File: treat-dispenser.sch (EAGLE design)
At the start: 39 parts, among them U1 MCP73831, U2 TPS61032, U3 ATMEGA32U4, Y1 16MHz

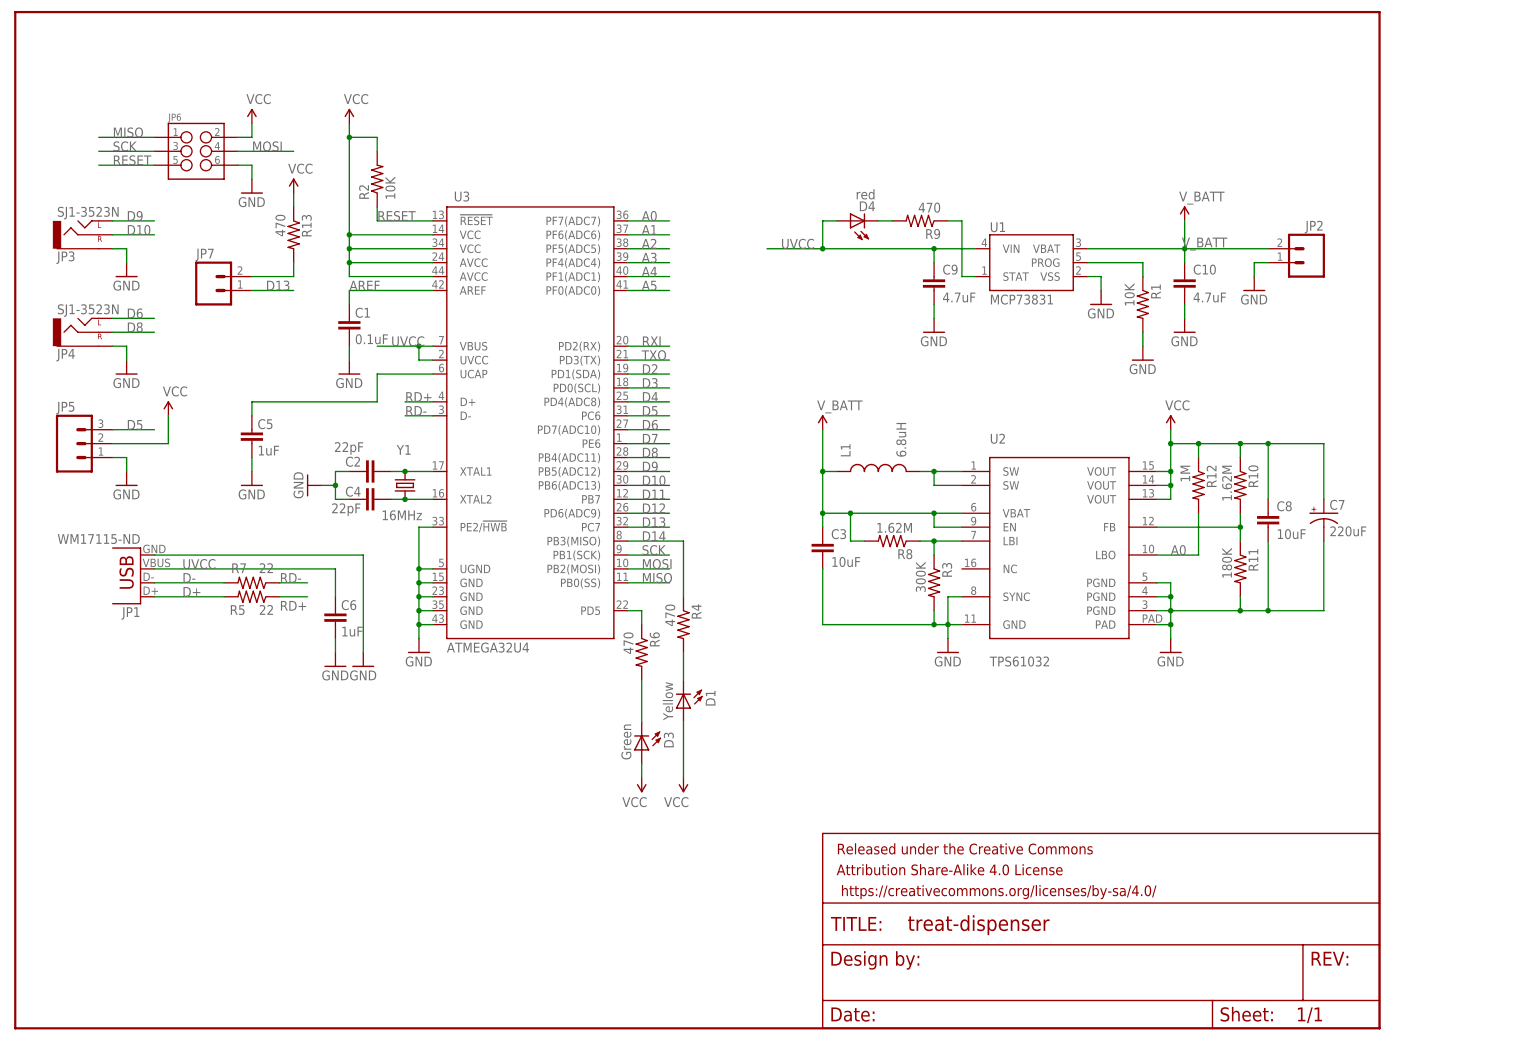
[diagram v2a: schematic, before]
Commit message: added optional sensor, cleaned up for mfg
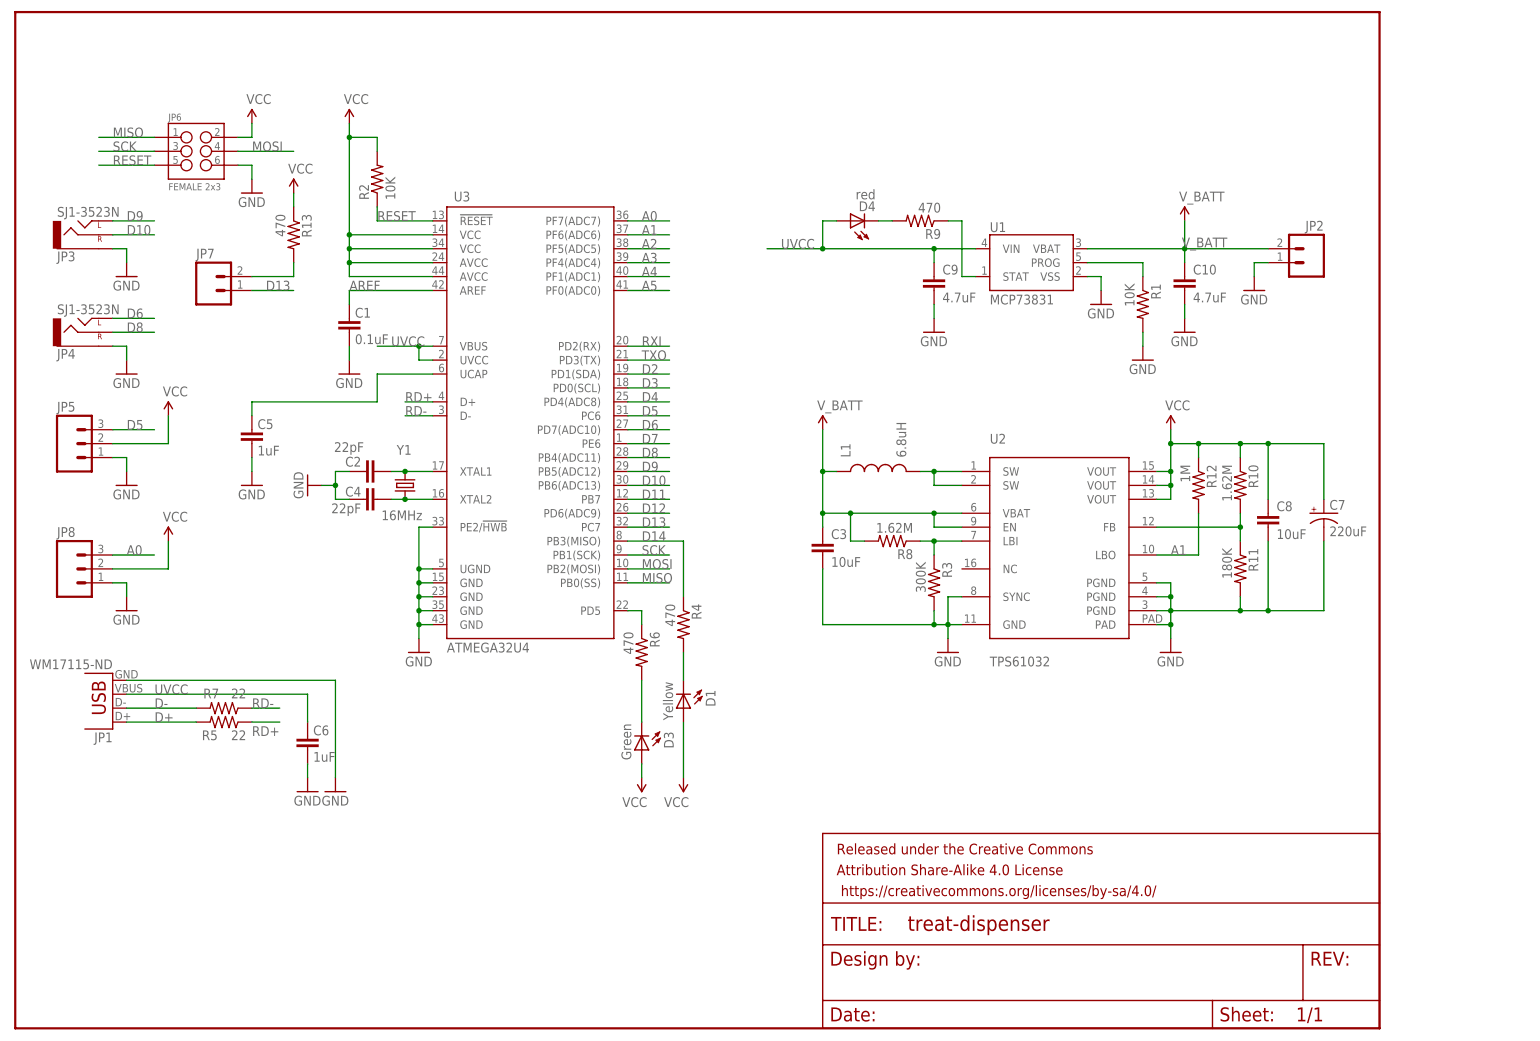
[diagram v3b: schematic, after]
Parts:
- added JP8: (no value), SparkFun-Connectors:M03PTH
- JP6: value (none) -> FEMALE 2x3; device SparkFun-Connectors:M03X2POGO_PINS -> SparkFun-Connectors:M03X2FEMALE
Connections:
- net A0: now also JP8.3; no longer R12.2, U2.LBO
- net A1: now also R12.2, U2.LBO
- net GND: now also JP8.1
- net VCC: now also JP8.2
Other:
- moved on the sheet: C6, JP1, R5, R7
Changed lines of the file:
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@@
 <part name="GND12" library="supply1" deviceset="GND" device=""/>
 <part name="R12" library="SparkFun" deviceset="RESISTOR" device="0603-RES" value="1M"/>
-<part name="JP6" library="SparkFun-Connectors" deviceset="M03X2" device="POGO_PINS"/>
 <part name="GND13" library="supply1" deviceset="GND" device=""/>
 <part name="C7" library="SparkFun-Capacitors" deviceset="CAP_POL" device="PTH1" value="220uF"/>
@@
 <part name="R13" library="SparkFun" deviceset="RESISTOR" device="0603-RES" value="470"/>
 <part name="SUPPLY7" library="SparkFun-Aesthetics" deviceset="VCC" device=""/>
+<part name="JP6" library="SparkFun-Connectors" deviceset="M03X2" device="FEMALE" value="FEMALE 2x3"/>
+<part name="JP8" library="SparkFun-Connectors" deviceset="M03" device="PTH"/>
+<part name="GND15" library="supply1" deviceset="GND" device=""/>
+<part name="SUPPLY8" library="SparkFun-Aesthetics" deviceset="VCC" device=""/>
 </parts>
 <sheets>
@@
 </instance>
 <instance part="GND6" gate="1" x="43.18" y="99.06"/>
-<instance part="C6" gate="G$1" x="58.42" y="76.2" smashed="yes" rot="R180">
-<attribute name="NAME" x="59.436" y="76.327" size="1.778" layer="95"/>
-<attribute name="VALUE" x="59.436" y="71.501" size="1.778" layer="96"/>
-</instance>
-<instance part="GND9" gate="1" x="58.42" y="66.04"/>
+<instance part="C6" gate="G$1" x="53.34" y="53.34" smashed="yes" rot="R180">
+<attribute name="NAME" x="54.356" y="53.467" size="1.778" layer="95"/>
+<attribute name="VALUE" x="54.356" y="48.641" size="1.778" layer="96"/>
+</instance>
+<instance part="GND9" gate="1" x="53.34" y="43.18"/>
 <instance part="R4" gate="G$1" x="121.92" y="73.66" rot="R270"/>
 <instance part="D1" gate="G$1" x="121.92" y="58.42" smashed="yes" rot="R180">
@@
 <attribute name="VALUE" x="118.237" y="63.246" size="1.778" layer="96" rot="R270"/>
 </instance>
-<instance part="R5" gate="G$1" x="43.18" y="78.74" smashed="yes" rot="R180">
-<attribute name="NAME" x="39.116" y="75.438" size="1.778" layer="95"/>
-<attribute name="VALUE" x="44.45" y="75.438" size="1.778" layer="96"/>
-</instance>
-<instance part="R7" gate="G$1" x="43.18" y="81.28" smashed="yes" rot="R180">
-<attribute name="NAME" x="39.37" y="83.058" size="1.778" layer="95"/>
-<attribute name="VALUE" x="44.45" y="83.058" size="1.778" layer="96"/>
-</instance>
-<instance part="GND3" gate="1" x="63.5" y="66.04"/>
+<instance part="R5" gate="G$1" x="38.1" y="55.88" smashed="yes" rot="R180">
+<attribute name="NAME" x="34.036" y="52.578" size="1.778" layer="95"/>
+<attribute name="VALUE" x="39.37" y="52.578" size="1.778" layer="96"/>
+</instance>
+<instance part="R7" gate="G$1" x="38.1" y="58.42" smashed="yes" rot="R180">
+<attribute name="NAME" x="34.29" y="60.198" size="1.778" layer="95"/>
+<attribute name="VALUE" x="39.37" y="60.198" size="1.778" layer="96"/>
+</instance>
+<instance part="GND3" gate="1" x="58.42" y="43.18"/>
 <instance part="P+1" gate="1" x="114.3" y="45.72" rot="R180"/>
 <instance part="P+2" gate="1" x="121.92" y="45.72" rot="R180"/>
-<instance part="JP1" gate="G$1" x="22.86" y="86.36" rot="R180"/>
+<instance part="JP1" gate="G$1" x="17.78" y="63.5" rot="R180"/>
 <instance part="C9" gate="G$1" x="167.64" y="134.62"/>
 <instance part="C10" gate="G$1" x="213.36" y="134.62"/>
@@
 <instance part="GND12" gate="1" x="20.32" y="137.16"/>
 <instance part="R12" gate="G$1" x="215.9" y="99.06" rot="R270"/>
-<instance part="JP6" gate="G$1" x="33.02" y="160.02"/>
 <instance part="GND13" gate="1" x="43.18" y="152.4"/>
 <instance part="C7" gate="G$1" x="238.76" y="93.98"/>
@@
 <instance part="R13" gate="G$1" x="50.8" y="144.78" rot="R270"/>
 <instance part="SUPPLY7" gate="G$1" x="50.8" y="152.4"/>
+<instance part="JP6" gate="G$1" x="33.02" y="160.02"/>
+<instance part="JP8" gate="G$1" x="10.16" y="83.82"/>
+<instance part="GND15" gate="1" x="20.32" y="76.2"/>
+<instance part="SUPPLY8" gate="G$1" x="27.94" y="88.9"/>
 </instances>
 <busses>
@@
 </segment>
 <segment>
-<wire x1="58.42" y1="71.12" x2="58.42" y2="68.58" width="0.1524" layer="91"/>
+<wire x1="53.34" y1="48.26" x2="53.34" y2="45.72" width="0.1524" layer="91"/>
 <pinref part="C6" gate="G$1" pin="1"/>
 <pinref part="GND9" gate="1" pin="GND"/>
 </segment>
 <segment>
-<wire x1="63.5" y1="86.36" x2="63.5" y2="68.58" width="0.1524" layer="91"/>
+<wire x1="58.42" y1="63.5" x2="58.42" y2="45.72" width="0.1524" layer="91"/>
 <pinref part="GND3" gate="1" pin="GND"/>
-<wire x1="63.5" y1="86.36" x2="25.4" y2="86.36" width="0.1524" layer="91"/>
+<wire x1="58.42" y1="63.5" x2="20.32" y2="63.5" width="0.1524" layer="91"/>
 <pinref part="JP1" gate="G$1" pin="GND"/>
 </segment>
@@
 </segment>
 <segment>
-<pinref part="JP6" gate="G$1" pin="6"/>
 <pinref part="GND13" gate="1" pin="GND"/>
 <wire x1="40.64" y1="157.48" x2="43.18" y2="157.48" width="0.1524" layer="91"/>
 <wire x1="43.18" y1="157.48" x2="43.18" y2="154.94" width="0.1524" layer="91"/>
+<pinref part="JP6" gate="G$1" pin="6"/>
+</segment>
+<segment>
+<pinref part="JP8" gate="G$1" pin="1"/>
+<pinref part="GND15" gate="1" pin="GND"/>
+<wire x1="17.78" y1="81.28" x2="20.32" y2="81.28" width="0.1524" layer="91"/>
+<wire x1="20.32" y1="81.28" x2="20.32" y2="78.74" width="0.1524" layer="91"/>
 </segment>
 </net>
@@
 </segment>
 <segment>
-<pinref part="JP6" gate="G$1" pin="5"/>
 <wire x1="25.4" y1="157.48" x2="15.24" y2="157.48" width="0.1524" layer="91"/>
 <label x="17.78" y="157.48" size="1.778" layer="95"/>
+<pinref part="JP6" gate="G$1" pin="5"/>
 </segment>
 </net>
@@
 </segment>
 <segment>
-<pinref part="JP6" gate="G$1" pin="3"/>
 <wire x1="25.4" y1="160.02" x2="15.24" y2="160.02" width="0.1524" layer="91"/>
 <label x="17.78" y="160.02" size="1.778" layer="95"/>
+<pinref part="JP6" gate="G$1" pin="3"/>
 </segment>
 </net>
@@
 </segment>
 <segment>
-<pinref part="JP6" gate="G$1" pin="1"/>
 <wire x1="25.4" y1="162.56" x2="15.24" y2="162.56" width="0.1524" layer="91"/>
 <label x="17.78" y="162.56" size="1.778" layer="95"/>
+<pinref part="JP6" gate="G$1" pin="1"/>
 </segment>
 </net>
@@
 </segment>
 <segment>
-<pinref part="JP6" gate="G$1" pin="4"/>
 <wire x1="40.64" y1="160.02" x2="50.8" y2="160.02" width="0.1524" layer="91"/>
 <label x="43.18" y="160.02" size="1.778" layer="95"/>
+<pinref part="JP6" gate="G$1" pin="4"/>
 </segment>
 </net>
@@
 <segment>
 <wire x1="43.18" y1="165.1" x2="43.18" y2="162.56" width="0.1524" layer="91"/>
-<pinref part="JP6" gate="G$1" pin="2"/>
 <wire x1="43.18" y1="162.56" x2="40.64" y2="162.56" width="0.1524" layer="91"/>
 <pinref part="SUPPLY5" gate="G$1" pin="VCC"/>
+<pinref part="JP6" gate="G$1" pin="2"/>
 </segment>
 <segment>
@@
 <wire x1="50.8" y1="149.86" x2="50.8" y2="152.4" width="0.1524" layer="91"/>
 </segment>
+<segment>
+<pinref part="JP8" gate="G$1" pin="2"/>
+<wire x1="17.78" y1="83.82" x2="27.94" y2="83.82" width="0.1524" layer="91"/>
+<wire x1="27.94" y1="83.82" x2="27.94" y2="88.9" width="0.1524" layer="91"/>
+<pinref part="SUPPLY8" gate="G$1" pin="VCC"/>
+</segment>
 </net>
 <net name="D9" class="0">
@@
 <label x="114.3" y="144.78" size="1.778" layer="95"/>
 <pinref part="U3" gate="G$1" pin="PF6(ADC6)"/>
-</segment>
-</net>
-<net name="A0" class="0">
-<segment>
-<wire x1="111.76" y1="147.32" x2="119.38" y2="147.32" width="0.1524" layer="91"/>
-<label x="114.3" y="147.32" size="1.778" layer="95"/>
-<pinref part="U3" gate="G$1" pin="PF7(ADC7)"/>
 </segment>
 <segment>
@@
 <wire x1="215.9" y1="86.36" x2="208.28" y2="86.36" width="0.1524" layer="91"/>
 <label x="210.82" y="86.36" size="1.778" layer="95"/>
+</segment>
+</net>
+<net name="A0" class="0">
+<segment>
+<wire x1="111.76" y1="147.32" x2="119.38" y2="147.32" width="0.1524" layer="91"/>
+<label x="114.3" y="147.32" size="1.778" layer="95"/>
+<pinref part="U3" gate="G$1" pin="PF7(ADC7)"/>
+</segment>
+<segment>
+<pinref part="JP8" gate="G$1" pin="3"/>
+<wire x1="17.78" y1="86.36" x2="25.4" y2="86.36" width="0.1524" layer="91"/>
+<label x="20.32" y="86.36" size="1.778" layer="95"/>
 </segment>
 </net>
@@
 <pinref part="R7" gate="G$1" pin="2"/>
 <pinref part="JP1" gate="G$1" pin="D-"/>
-<wire x1="38.1" y1="81.28" x2="25.4" y2="81.28" width="0.1524" layer="91"/>
-<label x="30.48" y="81.28" size="1.778" layer="95"/>
+<wire x1="33.02" y1="58.42" x2="20.32" y2="58.42" width="0.1524" layer="91"/>
+<label x="25.4" y="58.42" size="1.778" layer="95"/>
 </segment>
 </net>
@@
 <segment>
 <pinref part="R5" gate="G$1" pin="2"/>
-<wire x1="38.1" y1="78.74" x2="25.4" y2="78.74" width="0.1524" layer="91"/>
+<wire x1="33.02" y1="55.88" x2="20.32" y2="55.88" width="0.1524" layer="91"/>
 <pinref part="JP1" gate="G$1" pin="D+"/>
-<label x="30.48" y="78.74" size="1.778" layer="95"/>
+<label x="25.4" y="55.88" size="1.778" layer="95"/>
 </segment>
 </net>
@@
 <net name="UVCC" class="0">
 <segment>
-<label x="30.48" y="83.82" size="1.778" layer="95"/>
+<label x="25.4" y="60.96" size="1.778" layer="95"/>
 <pinref part="JP1" gate="G$1" pin="VBUS"/>
-<wire x1="58.42" y1="83.82" x2="58.42" y2="78.74" width="0.1524" layer="91"/>
+<wire x1="53.34" y1="60.96" x2="53.34" y2="55.88" width="0.1524" layer="91"/>
 <pinref part="C6" gate="G$1" pin="2"/>
-<wire x1="25.4" y1="83.82" x2="58.42" y2="83.82" width="0.1524" layer="91"/>
+<wire x1="20.32" y1="60.96" x2="53.34" y2="60.96" width="0.1524" layer="91"/>
 </segment>
 <segment>
@@
 <net name="RD-" class="0">
 <segment>
-<wire x1="48.26" y1="81.28" x2="53.34" y2="81.28" width="0.1524" layer="91"/>
-<label x="48.26" y="81.28" size="1.778" layer="95"/>
+<wire x1="43.18" y1="58.42" x2="48.26" y2="58.42" width="0.1524" layer="91"/>
+<label x="43.18" y="58.42" size="1.778" layer="95"/>
 <pinref part="R7" gate="G$1" pin="1"/>
 </segment>
@@
 <net name="RD+" class="0">
 <segment>
-<wire x1="48.26" y1="78.74" x2="53.34" y2="78.74" width="0.1524" layer="91"/>
-<label x="48.26" y="76.2" size="1.778" layer="95"/>
+<wire x1="43.18" y1="55.88" x2="48.26" y2="55.88" width="0.1524" layer="91"/>
+<label x="43.18" y="53.34" size="1.778" layer="95"/>
 <pinref part="R5" gate="G$1" pin="1"/>
 </segment>

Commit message: added part numbers for bom, manufacturing files
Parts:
- removed L1: 6.8uH, SparkFun-Passives:INDUCTOR0603
- added L2: (no value), SparkFun-Passives:INDUCTOR
- C1: PN (none) -> GRM188R61C104KA01D
- C10, C9: PN (none) -> GRM188R61C475KAAJD
- C2, C4: PN (none) -> GRM1885C2A220JA01D
- C3, C8: PN (none) -> GRM188C81C106MA73D
- C5, C6: PN (none) -> GRM188R61C105KA93D
- C7: PN (none) -> UVR1A221MED
- D1: PN (none) -> LTST-C190KSKT
- D3: PN (none) -> LTST-C190KGKT
- D4: PN (none) -> LTST-C190KRKT
- JP1: value WM17115-ND -> USB-MB-H; PN (none) -> WM17115-ND
- JP2: PN (none) -> S2B-PH-K-S(LF)(SN)
- JP3, JP4: value SJ1-3523N -> (none); PN (none) -> SJ1-3523N
- JP5, JP8: PN (none) -> M22-2510305
- JP6: value FEMALE 2x3 -> (none); PN (none) -> M20-9980346
- JP7: PN (none) -> M22-2510205
- R1, R2: PN (none) -> CR0603-JW-103ELF
- R10, R8: value 1.62M -> 1M; PN (none) -> CR0603-JW-105ELF
- R11: value 180K -> 110K; PN (none) -> CR0603-FX-1103ELF
- R12: PN (none) -> CR0603-JW-105ELF
- R13, R4, R6, R9: PN (none) -> CR0603-FX-4700ELF
- R3: value 300K -> 182K; PN (none) -> CR0603-FX-1823ELF
- R5, R7: PN (none) -> CR0603-JW-220ELF
- U1: PN (none) -> MCP73831T-2ATI/OT
- U2: value TPS61032 -> TPS6103x; PN (none) -> TPS61032PWPR
- U3: PN (none) -> ATMEGA32U4-AUR
- Y1: PN (none) -> ECS-160-S-4
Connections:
- net SW: now also L2.2; no longer L1.2
- net V_BATT: now also L2.1; no longer L1.1
